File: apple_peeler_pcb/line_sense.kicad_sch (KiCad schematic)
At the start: 4 parts, among them Q10 2N7002

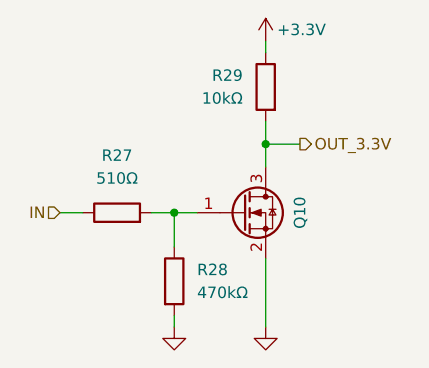
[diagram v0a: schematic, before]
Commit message: we paid for all the pins, we're gonna use all the pins
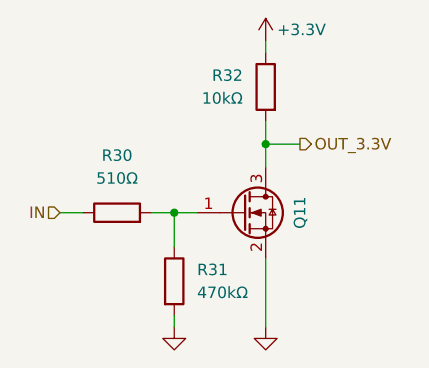
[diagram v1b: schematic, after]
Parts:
- renumbered Q10 to Q11, R27 to R30, R28 to R31, R29 to R32
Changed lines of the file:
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@@
 		(on_board yes)
 		(dnp no)
-		(property "Reference" "#PWR048"
+		(property "Reference" "#PWR040"
 			(at 135.89 116.84 0)
 			(effects
@@
 					(unit 1)
 				)
-				(path "/d5946b96-44a8-4a28-8641-19803e1510af/ab4760da-4146-4688-a275-418314974b55/fec152a4-11e6-4915-b614-693f728bc57e"
-					(reference "#PWR048")
+				(path "/d5946b96-44a8-4a28-8641-19803e1510af/ab4760da-4146-4688-a275-418314974b55/207d6e2c-5657-4cae-9098-bf31bbf0eeb3/9d425879-c049-4dfa-82be-004c8041dfbb"
+					(reference "#PWR040")
+					(unit 1)
+				)
+				(path "/d5946b96-44a8-4a28-8641-19803e1510af/ab4760da-4146-4688-a275-418314974b55/216077bc-1e97-451f-9a4f-0a4e0691e85e/9d425879-c049-4dfa-82be-004c8041dfbb"
+					(reference "#PWR0102")
 					(unit 1)
 				)
@@
 		(dnp no)
 		(fields_autoplaced yes)
-		(property "Reference" "R27"
+		(property "Reference" "R?"
 			(at 129.54 91.44 90)
 			(effects
@@
 					(unit 1)
 				)
-				(path "/d5946b96-44a8-4a28-8641-19803e1510af/ab4760da-4146-4688-a275-418314974b55/fec152a4-11e6-4915-b614-693f728bc57e"
-					(reference "R27")
+				(path "/d5946b96-44a8-4a28-8641-19803e1510af/ab4760da-4146-4688-a275-418314974b55/207d6e2c-5657-4cae-9098-bf31bbf0eeb3/9d425879-c049-4dfa-82be-004c8041dfbb"
+					(reference "R?")
+					(unit 1)
+				)
+				(path "/d5946b96-44a8-4a28-8641-19803e1510af/ab4760da-4146-4688-a275-418314974b55/216077bc-1e97-451f-9a4f-0a4e0691e85e/9d425879-c049-4dfa-82be-004c8041dfbb"
+					(reference "R?")
 					(unit 1)
 				)
@@
 		(dnp no)
 		(fields_autoplaced yes)
-		(property "Reference" "R29"
+		(property "Reference" "R?"
 			(at 143.51 82.5499 0)
 			(effects
@@
 					(unit 1)
 				)
-				(path "/d5946b96-44a8-4a28-8641-19803e1510af/ab4760da-4146-4688-a275-418314974b55/fec152a4-11e6-4915-b614-693f728bc57e"
-					(reference "R29")
+				(path "/d5946b96-44a8-4a28-8641-19803e1510af/ab4760da-4146-4688-a275-418314974b55/207d6e2c-5657-4cae-9098-bf31bbf0eeb3/9d425879-c049-4dfa-82be-004c8041dfbb"
+					(reference "R?")
+					(unit 1)
+				)
+				(path "/d5946b96-44a8-4a28-8641-19803e1510af/ab4760da-4146-4688-a275-418314974b55/216077bc-1e97-451f-9a4f-0a4e0691e85e/9d425879-c049-4dfa-82be-004c8041dfbb"
+					(reference "R?")
 					(unit 1)
 				)
@@
 		(on_board yes)
 		(dnp no)
-		(property "Reference" "#PWR050"
+		(property "Reference" "#PWR042"
 			(at 146.05 116.84 0)
 			(effects
@@
 					(unit 1)
 				)
-				(path "/d5946b96-44a8-4a28-8641-19803e1510af/ab4760da-4146-4688-a275-418314974b55/fec152a4-11e6-4915-b614-693f728bc57e"
-					(reference "#PWR050")
+				(path "/d5946b96-44a8-4a28-8641-19803e1510af/ab4760da-4146-4688-a275-418314974b55/207d6e2c-5657-4cae-9098-bf31bbf0eeb3/9d425879-c049-4dfa-82be-004c8041dfbb"
+					(reference "#PWR042")
+					(unit 1)
+				)
+				(path "/d5946b96-44a8-4a28-8641-19803e1510af/ab4760da-4146-4688-a275-418314974b55/216077bc-1e97-451f-9a4f-0a4e0691e85e/9d425879-c049-4dfa-82be-004c8041dfbb"
+					(reference "#PWR0104")
 					(unit 1)
 				)
@@
 		(dnp no)
 		(fields_autoplaced yes)
-		(property "Reference" "R28"
+		(property "Reference" "R?"
 			(at 138.43 104.1399 0)
 			(effects
@@
 					(unit 1)
 				)
-				(path "/d5946b96-44a8-4a28-8641-19803e1510af/ab4760da-4146-4688-a275-418314974b55/fec152a4-11e6-4915-b614-693f728bc57e"
-					(reference "R28")
+				(path "/d5946b96-44a8-4a28-8641-19803e1510af/ab4760da-4146-4688-a275-418314974b55/207d6e2c-5657-4cae-9098-bf31bbf0eeb3/9d425879-c049-4dfa-82be-004c8041dfbb"
+					(reference "R?")
+					(unit 1)
+				)
+				(path "/d5946b96-44a8-4a28-8641-19803e1510af/ab4760da-4146-4688-a275-418314974b55/216077bc-1e97-451f-9a4f-0a4e0691e85e/9d425879-c049-4dfa-82be-004c8041dfbb"
+					(reference "R?")
 					(unit 1)
 				)
@@
 		(on_board yes)
 		(dnp no)
-		(property "Reference" "Q10"
+		(property "Reference" "Q?"
 			(at 149.86 97.79 90)
 			(effects
@@
 					(unit 1)
 				)
-				(path "/d5946b96-44a8-4a28-8641-19803e1510af/ab4760da-4146-4688-a275-418314974b55/fec152a4-11e6-4915-b614-693f728bc57e"
-					(reference "Q10")
+				(path "/d5946b96-44a8-4a28-8641-19803e1510af/ab4760da-4146-4688-a275-418314974b55/207d6e2c-5657-4cae-9098-bf31bbf0eeb3/9d425879-c049-4dfa-82be-004c8041dfbb"
+					(reference "Q?")
+					(unit 1)
+				)
+				(path "/d5946b96-44a8-4a28-8641-19803e1510af/ab4760da-4146-4688-a275-418314974b55/216077bc-1e97-451f-9a4f-0a4e0691e85e/9d425879-c049-4dfa-82be-004c8041dfbb"
+					(reference "Q?")
 					(unit 1)
 				)
@@
 		(on_board yes)
 		(dnp no)
-		(property "Reference" "#PWR049"
+		(property "Reference" "#PWR041"
 			(at 146.05 82.55 0)
 			(effects
@@
 					(unit 1)
 				)
-				(path "/d5946b96-44a8-4a28-8641-19803e1510af/ab4760da-4146-4688-a275-418314974b55/fec152a4-11e6-4915-b614-693f728bc57e"
-					(reference "#PWR049")
-					(unit 1)
-				)
+				(path "/d5946b96-44a8-4a28-8641-19803e1510af/ab4760da-4146-4688-a275-418314974b55/207d6e2c-5657-4cae-9098-bf31bbf0eeb3/9d425879-c049-4dfa-82be-004c8041dfbb"
+					(reference "#PWR041")
+					(unit 1)
+				)
+				(path "/d5946b96-44a8-4a28-8641-19803e1510af/ab4760da-4146-4688-a275-418314974b55/216077bc-1e97-451f-9a4f-0a4e0691e85e/9d425879-c049-4dfa-82be-004c8041dfbb"
+					(reference "#PWR0103")
+					(unit 1)
+				)

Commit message: use wleds instead of individual leds
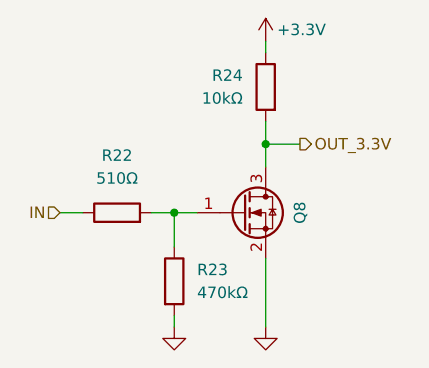
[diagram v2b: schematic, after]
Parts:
- renumbered Q11 to Q8, R30 to R22, R31 to R23, R32 to R24
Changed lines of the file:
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@@
 		(on_board yes)
 		(dnp no)
-		(property "Reference" "#PWR040"
+		(property "Reference" "#PWR043"
 			(at 135.89 116.84 0)
 			(effects
@@
 			(project "apple_peeler_pcb"
 				(path "/d5946b96-44a8-4a28-8641-19803e1510af/ab4760da-4146-4688-a275-418314974b55/657a47b5-711a-4c36-9b6b-73aa4928b137"
-					(reference "#PWR051")
-					(unit 1)
-				)
-				(path "/d5946b96-44a8-4a28-8641-19803e1510af/ab4760da-4146-4688-a275-418314974b55/207d6e2c-5657-4cae-9098-bf31bbf0eeb3/9d425879-c049-4dfa-82be-004c8041dfbb"
-					(reference "#PWR040")
-					(unit 1)
-				)
-				(path "/d5946b96-44a8-4a28-8641-19803e1510af/ab4760da-4146-4688-a275-418314974b55/216077bc-1e97-451f-9a4f-0a4e0691e85e/9d425879-c049-4dfa-82be-004c8041dfbb"
-					(reference "#PWR0102")
+					(reference "#PWR046")
+					(unit 1)
+				)
+				(path "/d5946b96-44a8-4a28-8641-19803e1510af/ab4760da-4146-4688-a275-418314974b55/207d6e2c-5657-4cae-9098-bf31bbf0eeb3/9d425879-c049-4dfa-82be-004c8041dfbb"
+					(reference "#PWR043")
+					(unit 1)
+				)
+				(path "/d5946b96-44a8-4a28-8641-19803e1510af/ab4760da-4146-4688-a275-418314974b55/216077bc-1e97-451f-9a4f-0a4e0691e85e/9d425879-c049-4dfa-82be-004c8041dfbb"
+					(reference "#PWR095")
 					(unit 1)
 				)
@@
 		(dnp no)
 		(fields_autoplaced yes)
-		(property "Reference" "R?"
+		(property "Reference" "R22"
 			(at 129.54 91.44 90)
 			(effects
@@
 			(project "apple_peeler_pcb"
 				(path "/d5946b96-44a8-4a28-8641-19803e1510af/ab4760da-4146-4688-a275-418314974b55/657a47b5-711a-4c36-9b6b-73aa4928b137"
-					(reference "R30")
-					(unit 1)
-				)
-				(path "/d5946b96-44a8-4a28-8641-19803e1510af/ab4760da-4146-4688-a275-418314974b55/207d6e2c-5657-4cae-9098-bf31bbf0eeb3/9d425879-c049-4dfa-82be-004c8041dfbb"
-					(reference "R?")
-					(unit 1)
-				)
-				(path "/d5946b96-44a8-4a28-8641-19803e1510af/ab4760da-4146-4688-a275-418314974b55/216077bc-1e97-451f-9a4f-0a4e0691e85e/9d425879-c049-4dfa-82be-004c8041dfbb"
-					(reference "R?")
+					(reference "R25")
+					(unit 1)
+				)
+				(path "/d5946b96-44a8-4a28-8641-19803e1510af/ab4760da-4146-4688-a275-418314974b55/207d6e2c-5657-4cae-9098-bf31bbf0eeb3/9d425879-c049-4dfa-82be-004c8041dfbb"
+					(reference "R22")
+					(unit 1)
+				)
+				(path "/d5946b96-44a8-4a28-8641-19803e1510af/ab4760da-4146-4688-a275-418314974b55/216077bc-1e97-451f-9a4f-0a4e0691e85e/9d425879-c049-4dfa-82be-004c8041dfbb"
+					(reference "R44")
 					(unit 1)
 				)
@@
 		(dnp no)
 		(fields_autoplaced yes)
-		(property "Reference" "R?"
+		(property "Reference" "R24"
 			(at 143.51 82.5499 0)
 			(effects
@@
 			(project "apple_peeler_pcb"
 				(path "/d5946b96-44a8-4a28-8641-19803e1510af/ab4760da-4146-4688-a275-418314974b55/657a47b5-711a-4c36-9b6b-73aa4928b137"
-					(reference "R32")
-					(unit 1)
-				)
-				(path "/d5946b96-44a8-4a28-8641-19803e1510af/ab4760da-4146-4688-a275-418314974b55/207d6e2c-5657-4cae-9098-bf31bbf0eeb3/9d425879-c049-4dfa-82be-004c8041dfbb"
-					(reference "R?")
-					(unit 1)
-				)
-				(path "/d5946b96-44a8-4a28-8641-19803e1510af/ab4760da-4146-4688-a275-418314974b55/216077bc-1e97-451f-9a4f-0a4e0691e85e/9d425879-c049-4dfa-82be-004c8041dfbb"
-					(reference "R?")
+					(reference "R27")
+					(unit 1)
+				)
+				(path "/d5946b96-44a8-4a28-8641-19803e1510af/ab4760da-4146-4688-a275-418314974b55/207d6e2c-5657-4cae-9098-bf31bbf0eeb3/9d425879-c049-4dfa-82be-004c8041dfbb"
+					(reference "R24")
+					(unit 1)
+				)
+				(path "/d5946b96-44a8-4a28-8641-19803e1510af/ab4760da-4146-4688-a275-418314974b55/216077bc-1e97-451f-9a4f-0a4e0691e85e/9d425879-c049-4dfa-82be-004c8041dfbb"
+					(reference "R46")
 					(unit 1)
 				)
@@
 		(on_board yes)
 		(dnp no)
-		(property "Reference" "#PWR042"
+		(property "Reference" "#PWR045"
 			(at 146.05 116.84 0)
 			(effects
@@
 			(project "apple_peeler_pcb"
 				(path "/d5946b96-44a8-4a28-8641-19803e1510af/ab4760da-4146-4688-a275-418314974b55/657a47b5-711a-4c36-9b6b-73aa4928b137"
-					(reference "#PWR053")
-					(unit 1)
-				)
-				(path "/d5946b96-44a8-4a28-8641-19803e1510af/ab4760da-4146-4688-a275-418314974b55/207d6e2c-5657-4cae-9098-bf31bbf0eeb3/9d425879-c049-4dfa-82be-004c8041dfbb"
-					(reference "#PWR042")
-					(unit 1)
-				)
-				(path "/d5946b96-44a8-4a28-8641-19803e1510af/ab4760da-4146-4688-a275-418314974b55/216077bc-1e97-451f-9a4f-0a4e0691e85e/9d425879-c049-4dfa-82be-004c8041dfbb"
-					(reference "#PWR0104")
+					(reference "#PWR048")
+					(unit 1)
+				)
+				(path "/d5946b96-44a8-4a28-8641-19803e1510af/ab4760da-4146-4688-a275-418314974b55/207d6e2c-5657-4cae-9098-bf31bbf0eeb3/9d425879-c049-4dfa-82be-004c8041dfbb"
+					(reference "#PWR045")
+					(unit 1)
+				)
+				(path "/d5946b96-44a8-4a28-8641-19803e1510af/ab4760da-4146-4688-a275-418314974b55/216077bc-1e97-451f-9a4f-0a4e0691e85e/9d425879-c049-4dfa-82be-004c8041dfbb"
+					(reference "#PWR097")
 					(unit 1)
 				)
@@
 		(dnp no)
 		(fields_autoplaced yes)
-		(property "Reference" "R?"
+		(property "Reference" "R23"
 			(at 138.43 104.1399 0)
 			(effects
@@
 			(project "apple_peeler_pcb"
 				(path "/d5946b96-44a8-4a28-8641-19803e1510af/ab4760da-4146-4688-a275-418314974b55/657a47b5-711a-4c36-9b6b-73aa4928b137"
-					(reference "R31")
-					(unit 1)
-				)
-				(path "/d5946b96-44a8-4a28-8641-19803e1510af/ab4760da-4146-4688-a275-418314974b55/207d6e2c-5657-4cae-9098-bf31bbf0eeb3/9d425879-c049-4dfa-82be-004c8041dfbb"
-					(reference "R?")
-					(unit 1)
-				)
-				(path "/d5946b96-44a8-4a28-8641-19803e1510af/ab4760da-4146-4688-a275-418314974b55/216077bc-1e97-451f-9a4f-0a4e0691e85e/9d425879-c049-4dfa-82be-004c8041dfbb"
-					(reference "R?")
+					(reference "R26")
+					(unit 1)
+				)
+				(path "/d5946b96-44a8-4a28-8641-19803e1510af/ab4760da-4146-4688-a275-418314974b55/207d6e2c-5657-4cae-9098-bf31bbf0eeb3/9d425879-c049-4dfa-82be-004c8041dfbb"
+					(reference "R23")
+					(unit 1)
+				)
+				(path "/d5946b96-44a8-4a28-8641-19803e1510af/ab4760da-4146-4688-a275-418314974b55/216077bc-1e97-451f-9a4f-0a4e0691e85e/9d425879-c049-4dfa-82be-004c8041dfbb"
+					(reference "R45")
 					(unit 1)
 				)
@@
 		(on_board yes)
 		(dnp no)
-		(property "Reference" "Q?"
+		(property "Reference" "Q8"
 			(at 149.86 97.79 90)
 			(effects
@@
 			(project "apple_peeler_pcb"
 				(path "/d5946b96-44a8-4a28-8641-19803e1510af/ab4760da-4146-4688-a275-418314974b55/657a47b5-711a-4c36-9b6b-73aa4928b137"
-					(reference "Q11")
-					(unit 1)
-				)
-				(path "/d5946b96-44a8-4a28-8641-19803e1510af/ab4760da-4146-4688-a275-418314974b55/207d6e2c-5657-4cae-9098-bf31bbf0eeb3/9d425879-c049-4dfa-82be-004c8041dfbb"
-					(reference "Q?")
-					(unit 1)
-				)
-				(path "/d5946b96-44a8-4a28-8641-19803e1510af/ab4760da-4146-4688-a275-418314974b55/216077bc-1e97-451f-9a4f-0a4e0691e85e/9d425879-c049-4dfa-82be-004c8041dfbb"
-					(reference "Q?")
+					(reference "Q9")
+					(unit 1)
+				)
+				(path "/d5946b96-44a8-4a28-8641-19803e1510af/ab4760da-4146-4688-a275-418314974b55/207d6e2c-5657-4cae-9098-bf31bbf0eeb3/9d425879-c049-4dfa-82be-004c8041dfbb"
+					(reference "Q8")
+					(unit 1)
+				)
+				(path "/d5946b96-44a8-4a28-8641-19803e1510af/ab4760da-4146-4688-a275-418314974b55/216077bc-1e97-451f-9a4f-0a4e0691e85e/9d425879-c049-4dfa-82be-004c8041dfbb"
+					(reference "Q12")
 					(unit 1)
 				)
@@
 		(on_board yes)
 		(dnp no)
-		(property "Reference" "#PWR041"
+		(property "Reference" "#PWR044"
 			(at 146.05 82.55 0)
 			(effects
@@
 			(project "apple_peeler_pcb"
 				(path "/d5946b96-44a8-4a28-8641-19803e1510af/ab4760da-4146-4688-a275-418314974b55/657a47b5-711a-4c36-9b6b-73aa4928b137"
-					(reference "#PWR052")
-					(unit 1)
-				)
-				(path "/d5946b96-44a8-4a28-8641-19803e1510af/ab4760da-4146-4688-a275-418314974b55/207d6e2c-5657-4cae-9098-bf31bbf0eeb3/9d425879-c049-4dfa-82be-004c8041dfbb"
-					(reference "#PWR041")
-					(unit 1)
-				)
-				(path "/d5946b96-44a8-4a28-8641-19803e1510af/ab4760da-4146-4688-a275-418314974b55/216077bc-1e97-451f-9a4f-0a4e0691e85e/9d425879-c049-4dfa-82be-004c8041dfbb"
-					(reference "#PWR0103")
-					(unit 1)
-				)
+					(reference "#PWR047")
+					(unit 1)
+				)
+				(path "/d5946b96-44a8-4a28-8641-19803e1510af/ab4760da-4146-4688-a275-418314974b55/207d6e2c-5657-4cae-9098-bf31bbf0eeb3/9d425879-c049-4dfa-82be-004c8041dfbb"
+					(reference "#PWR044")
+					(unit 1)
+				)
+				(path "/d5946b96-44a8-4a28-8641-19803e1510af/ab4760da-4146-4688-a275-418314974b55/216077bc-1e97-451f-9a4f-0a4e0691e85e/9d425879-c049-4dfa-82be-004c8041dfbb"
+					(reference "#PWR096")
+					(unit 1)
+				)
